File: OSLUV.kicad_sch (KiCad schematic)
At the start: 6 parts, among them J6 B5P-VH

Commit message: Final Version Rev. 2.0.0
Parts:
- removed H1, H2: MountingHole_Pad, Hansmann:Mounting_M3_NPTH_Vias, symbol Mechanical:MountingHole_Pad
- removed ST1: 643495-2, Hansmann:643495-2, symbol Hansmann:643495-2_
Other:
- removed sheet offlineConverter
- sheet excimerDriver ports: added none; removed GND, VDC
- moved on the sheet: H3, H4

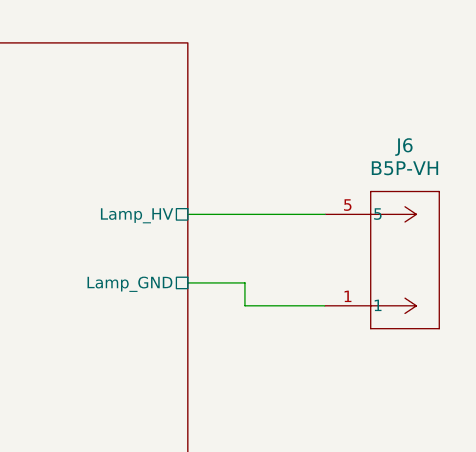
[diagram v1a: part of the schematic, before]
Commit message: Fixed BoM, and added jobset.
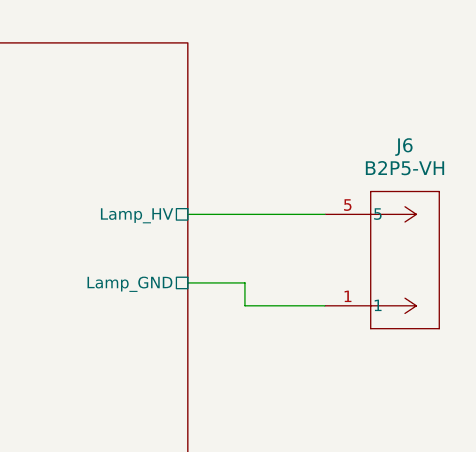
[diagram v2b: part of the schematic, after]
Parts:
- J6: value B5P-VH -> B2P5-VH; LCSC Part Number (none) -> C594162; Manufacturer_Part_Number (none) -> B2P5-VH
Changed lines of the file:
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@@
+			)
+		)
+		(property "LCSC Part Number" ""
+			(at 193.04 120.65 0)
+			(effects
+				(font
+					(size 1.27 1.27)
+				)
+				(hide yes)
 			)
 		)
@@
 			)
 		)
-		(property "Value" "B5P-VH"
+		(property "Value" "B2P5-VH"
 			(at 247.65 81.28 0)
 			(effects
@@
 		)
 		(property "VT (V (AC))" ""
+			(at 238.76 96.52 0)
+			(effects
+				(font
+					(size 1.27 1.27)
+				)
+				(hide yes)
+			)
+		)
+		(property "LCSC Part Number" "C594162"
+			(at 238.76 96.52 0)
+			(effects
+				(font
+					(size 1.27 1.27)
+				)
+				(hide yes)
+			)
+		)
+		(property "Manufacturer_Part_Number" "B2P5-VH"
 			(at 238.76 96.52 0)
 			(effects
@@
 			(at 182.88 120.65 0)
 			(effects
+				(font
+					(size 1.27 1.27)
+				)
+				(hide yes)
+			)
+		)
+		(property "LCSC Part Number" ""
+			(at 182.88 120.65 0)
+			(effects
